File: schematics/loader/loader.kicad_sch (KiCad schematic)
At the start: 16 parts, among them J1 Bus, J2 Bus, J4 to Microcode, SW1 RESET, U1 74HC595, U2 74LS00, U3 74HC595, U4 DM-OLED096-636

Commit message: Change Loader reset button
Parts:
- SW1: footprint Button_Switch_THT:SW_PUSH_6mm -> Button_Switch_THT:SW_PUSH-12mm
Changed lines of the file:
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@@
 			)
 		)
-		(property "Footprint" "Button_Switch_THT:SW_PUSH_6mm"
+		(property "Footprint" "Button_Switch_THT:SW_PUSH-12mm"
 			(at 110.49 157.48 0)
 			(effects

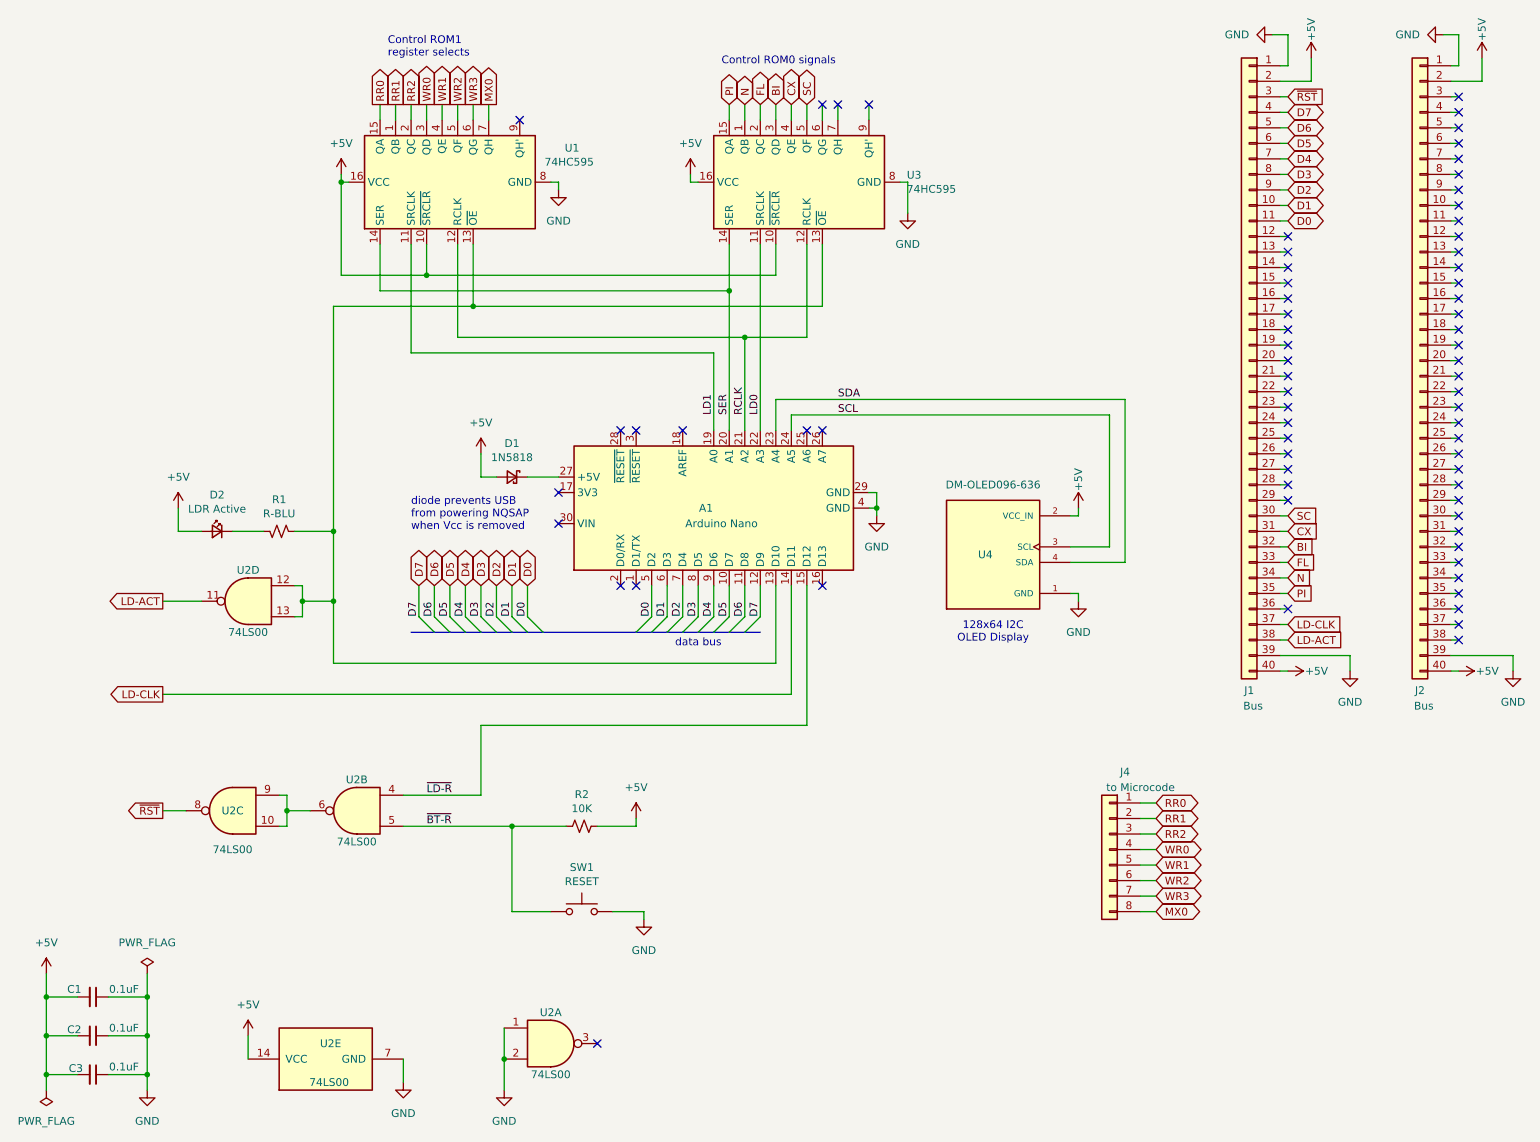
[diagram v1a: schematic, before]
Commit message: Arduino Loader Module v1.2 schematics and code
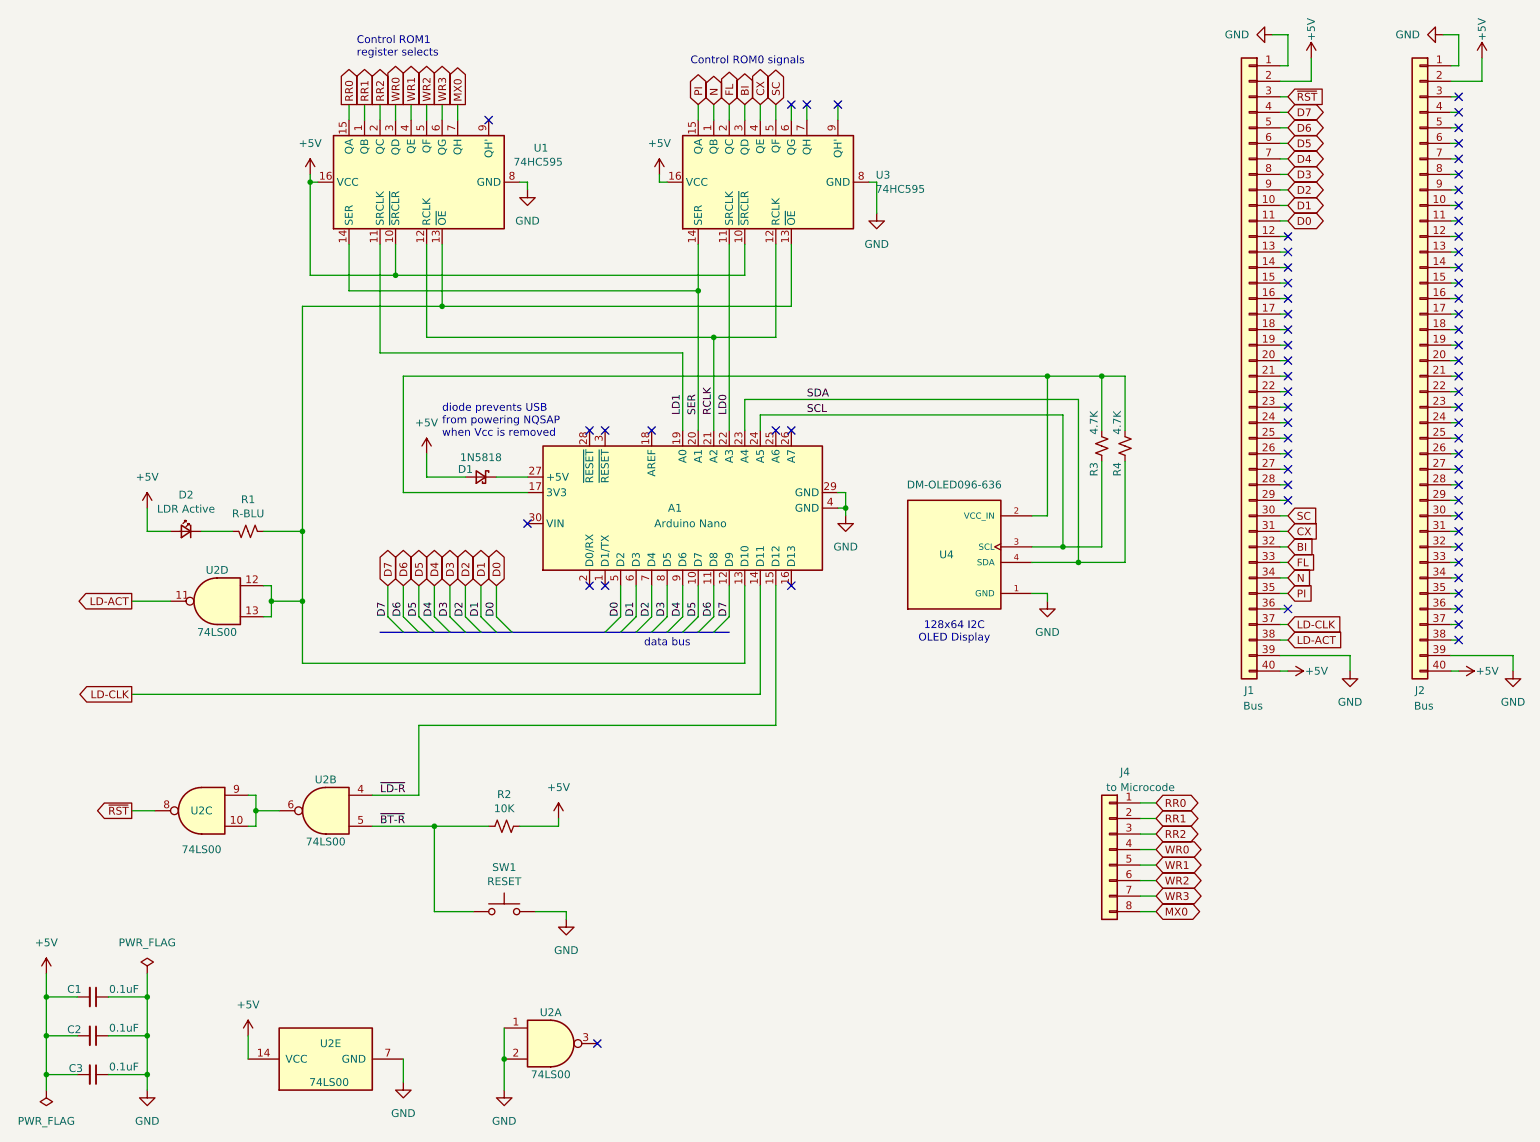
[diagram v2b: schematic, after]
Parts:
- added R3, R4: 4.7K, Resistor_THT:R_Axial_DIN0207_L6.3mm_D2.5mm_P10.16mm_Horizontal, symbol Device:R_Small_US
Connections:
- net +5V: no longer U4.2 (VCC_IN)
- net SCL: now also R3.2
- net SDA: now also R4.2
- net at A1.17 (3V3): now also U4.2 (VCC_IN), R3.1, R4.1
- no-connect marks 70 -> 69
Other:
- moved on the sheet: A1, D1, D2, R1, R2, SW1, U1, U2B, U2C, U2D, U3, U4
